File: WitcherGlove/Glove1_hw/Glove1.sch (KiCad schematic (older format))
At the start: 67 parts, among them M1 MOTOR, Q1 MMBT2222

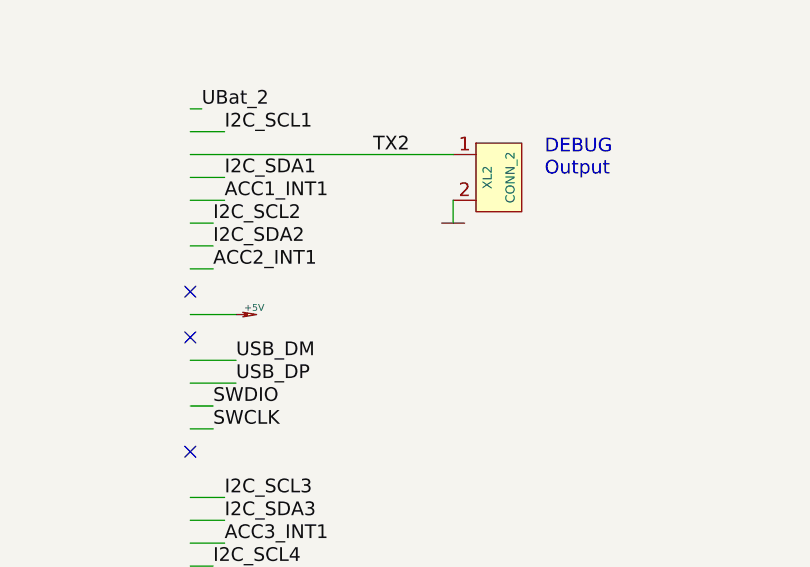
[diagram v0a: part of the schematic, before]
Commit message: Led added
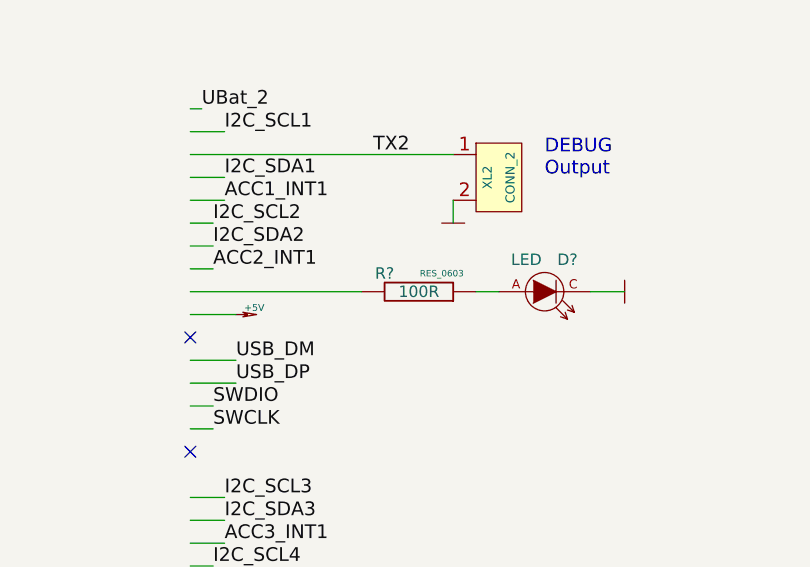
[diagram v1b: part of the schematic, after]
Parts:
- added D?: LED, symbol LED
- added R?: 100R, RES_0603, symbol R
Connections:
- wire segments 241 -> 244
- no-connect marks 11 -> 10

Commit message: 
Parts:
- gave numbers to parts that had none: 2
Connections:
- net labels added: ACC_PWR
- wire segments 244 -> 246
- no-connect marks 10 -> 9
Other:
- note added: "Peripherals usage\n\nUSB\nUART2 - debug output\nTIM1, TIM4 - LEDs"
- note removed: "Peripherals usage\n\nUSB\n??UART1 - debug output\nTIM4 - LEDs"

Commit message: 
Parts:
- added SW1: SWITCH, symbol SWITCH
- added XL7: CONN_4, symbol CONN_4
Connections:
- net labels added: B, BAT_TO_SW, G, R
- wire segments 246 -> 254
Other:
- moved on the sheet: D1, D2, D3, D4, XL6

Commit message: Demonstration of charge level at startup implemented
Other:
- note added: "BLUE"
- note added: "GREEN"
- note added: "RED"
- note added: "UV"
- note added: "YELLOW"

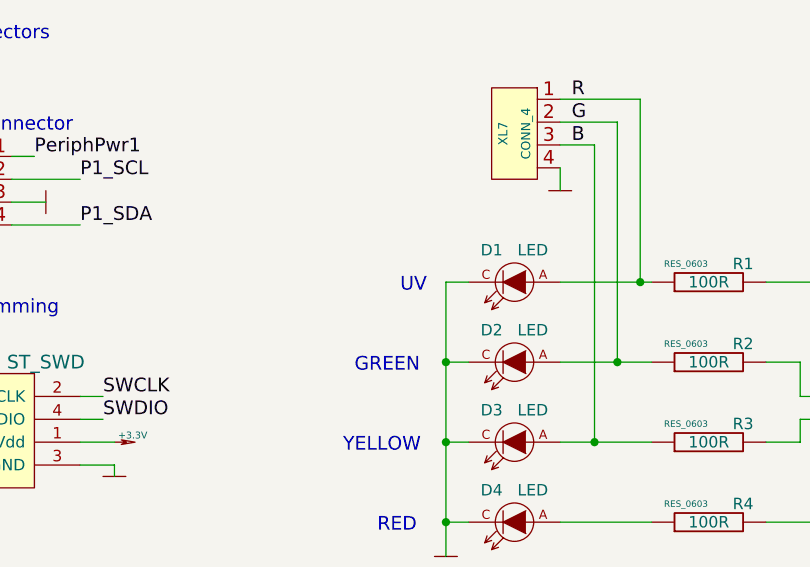
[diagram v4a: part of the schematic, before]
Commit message: Train mode added. Fixed printing of large amounts of data by adding chSysLock at printf function
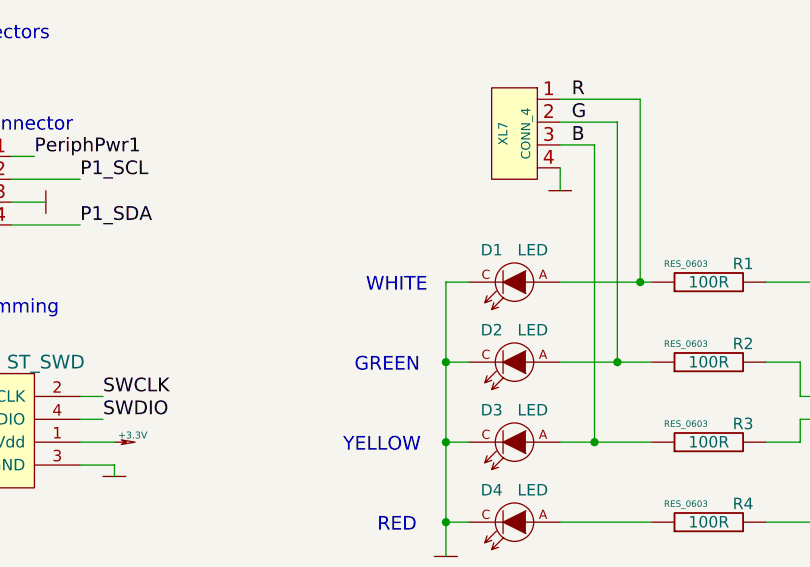
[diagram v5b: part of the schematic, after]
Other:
- note added: "WHITE"
- note removed: "UV"
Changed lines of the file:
@@
-EESchema Schematic File Version 2  date 07/07/2013 21:27:00
+EESchema Schematic File Version 2  date 10/08/2013 13:14:56
 LIBS:Connectors_kl
 LIBS:display_kl
@@
 Sheet 1 1
 Title ""
-Date "7 jul 2013"
+Date "9 aug 2013"
 Rev ""
 Comp ""
@@
 Text Notes 2600 2700 0    60   ~ 0
 YELLOW
-Text Notes 2850 2000 0    60   ~ 0
-UV
+Text Notes 2700 2000 0    60   ~ 0
+WHITE
 Text Notes 11050 2550 0    60   ~ 0
 BLUE
